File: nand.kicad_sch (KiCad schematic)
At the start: 5 parts, among them U6 IS21ES08GA-JQLI-TR

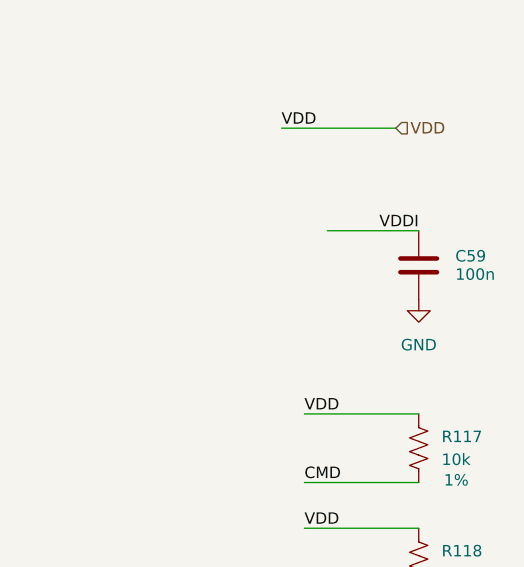
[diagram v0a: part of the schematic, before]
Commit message: Roughly placed all components
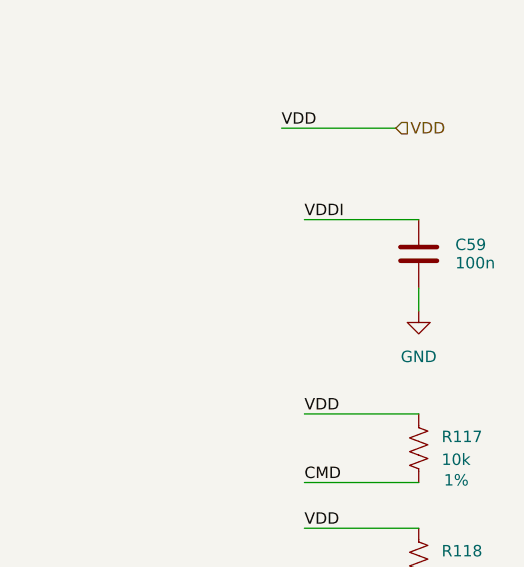
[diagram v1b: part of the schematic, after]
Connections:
- net GND: now also C59.2
- net VDDI: now also C59.1
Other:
- moved on the sheet: C59
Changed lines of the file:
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@@
 	(wire
 		(pts
-			(xy 246.3918 71.0847) (xy 256.5518 71.0847)
+			(xy 243.84 69.85) (xy 256.54 69.85)
 		)
 		(stroke
@@
 		(pts
 			(xy 168.91 101.6) (xy 168.91 104.14)
+		)
+		(stroke
+			(width 0)
+			(type default)
+		)
+	)
+	(wire
+		(pts
+			(xy 256.54 77.47) (xy 256.54 80.01)
 		)
 		(stroke
@@
 	)
 	(label "VDDI"
-		(at 256.5518 71.0847 180)
-		(fields_autoplaced yes)
-		(effects
-			(font
-				(size 1.27 1.27)
-			)
-			(justify right bottom)
+		(at 243.84 69.85 0)
+		(fields_autoplaced yes)
+		(effects
+			(font
+				(size 1.27 1.27)
+			)
+			(justify left bottom)
 		)
 	)
@@
 			)
 			(justify left)
+		)
+	)
+	(symbol
+		(lib_id "power:GND")
+		(at 256.54 80.01 0)
+		(unit 1)
+		(exclude_from_sim no)
+		(in_bom yes)
+		(on_board yes)
+		(dnp no)
+		(fields_autoplaced yes)
+		(property "Reference" "#PWR0218"
+			(at 256.54 86.36 0)
+			(effects
+				(font
+					(size 1.27 1.27)
+				)
+				(hide yes)
+			)
+		)
+		(property "Value" "GND"
+			(at 256.54 85.09 0)
+			(effects
+				(font
+					(size 1.27 1.27)
+				)
+			)
+		)
+		(property "Footprint" ""
+			(at 256.54 80.01 0)
+			(effects
+				(font
+					(size 1.27 1.27)
+				)
+				(hide yes)
+			)
+		)
+		(property "Datasheet" ""
+			(at 256.54 80.01 0)
+			(effects
+				(font
+					(size 1.27 1.27)
+				)
+				(hide yes)
+			)
+		)
+		(property "Description" "Power symbol creates a global label with name \"GND\" , ground"
+			(at 256.54 80.01 0)
+			(effects
+				(font
+					(size 1.27 1.27)
+				)
+				(hide yes)
+			)
+		)
+		(pin "1"
+		)
+		(instances
+			(project "SBC"
+				(path "/21bb932a-ec67-4661-9215-0551f718d1c0/dbc4538f-6782-4334-8773-c54462e4bd8b"
+					(reference "#PWR0218")
+					(unit 1)
+				)
+			)
 		)
 	)
@@
 	(symbol
 		(lib_id "SparkFun-Capacitor:C")
-		(at 256.54 74.93 0)
+		(at 256.54 73.66 0)
 		(unit 1)
 		(exclude_from_sim no)
@@
 		(dnp no)
 		(property "Reference" "C59"
-			(at 260.604 73.914 0)
+			(at 260.604 72.644 0)
 			(effects
 				(font
@@
 		)
 		(property "Value" "100n"
-			(at 260.604 75.946 0)
+			(at 260.604 74.676 0)
 			(effects
 				(font
@@
 		)
 		(property "Footprint" "Capacitor_SMD:C_0402_1005Metric"
-			(at 257.5052 86.36 0)
+			(at 257.5052 85.09 0)
 			(effects
 				(font
@@
 		)
 		(property "Datasheet" ""
-			(at 257.81 91.44 0)
+			(at 257.81 90.17 0)
 			(effects
 				(font
@@
 		)
 		(property "Description" "Unpolarized capacitor"
-			(at 256.54 93.98 0)
+			(at 256.54 92.71 0)
 			(effects
 				(font
@@
 		)
 		(property "PROD_ID" "CAP-00000"
-			(at 256.54 88.9 0)
+			(at 256.54 87.63 0)
 			(effects
 				(font
@@
 		)
 		(property "Voltage" ""
-			(at 260.35 76.1999 0)
+			(at 260.35 74.9299 0)
 			(effects
 				(font
@@
 					(unit 1)
 				)
-			)
-		)
-	)
-	(symbol
-		(lib_id "power:GND")
-		(at 256.5518 78.7047 0)
-		(unit 1)
-		(exclude_from_sim no)
-		(in_bom yes)
-		(on_board yes)
-		(dnp no)
-		(fields_autoplaced yes)
-		(property "Reference" "#PWR0218"
-			(at 256.5518 85.0547 0)
-			(effects
-				(font
-					(size 1.27 1.27)
-				)
-				(hide yes)
-			)
-		)
-		(property "Value" "GND"
-			(at 256.5518 83.7847 0)
-			(effects
-				(font
-					(size 1.27 1.27)
-				)
-			)
-		)
-		(property "Footprint" ""
-			(at 256.5518 78.7047 0)
-			(effects
-				(font
-					(size 1.27 1.27)
-				)
-				(hide yes)
-			)
-		)
-		(property "Datasheet" ""
-			(at 256.5518 78.7047 0)
-			(effects
-				(font
-					(size 1.27 1.27)
-				)
-				(hide yes)
-			)
-		)
-		(property "Description" "Power symbol creates a global label with name \"GND\" , ground"
-			(at 256.5518 78.7047 0)
-			(effects
-				(font
-					(size 1.27 1.27)
-				)
-				(hide yes)
-			)
-		)
-		(pin "1"
-		)
-		(instances
-			(project "SBC"
-				(path "/21bb932a-ec67-4661-9215-0551f718d1c0/dbc4538f-6782-4334-8773-c54462e4bd8b"
-					(reference "#PWR0218")
-					(unit 1)
-				)

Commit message: Routing routing routing
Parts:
- removed C59: 100n, Capacitor_SMD:C_0402_1005Metric, symbol SparkFun-Capacitor:C
- added C89, C90: 4.7u, Capacitor_SMD:C_0603_1608Metric, symbol SparkFun-Capacitor:C
- added C91: 1uF, Capacitor_SMD:C_0402_1005Metric, symbol SparkFun-Capacitor:C
- added R145: 10k, Capacitor_SMD:C_0402_1005Metric, symbol SparkFun-Resistor:R
- R117, R118, R119: Precision 1% -> 5%
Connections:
- net GND: now also C89.2, C90.2, C91.2, R145.2
- net VDD: now also C89.1, C90.1; no longer U6.E4 (VDDI)
- net VDDI: now also U6.E4 (VDDI), C91.1
- net DS: now reaches U6.K5 (DS)
- net DS: now also R145.1
- no-connect marks 1 -> 0

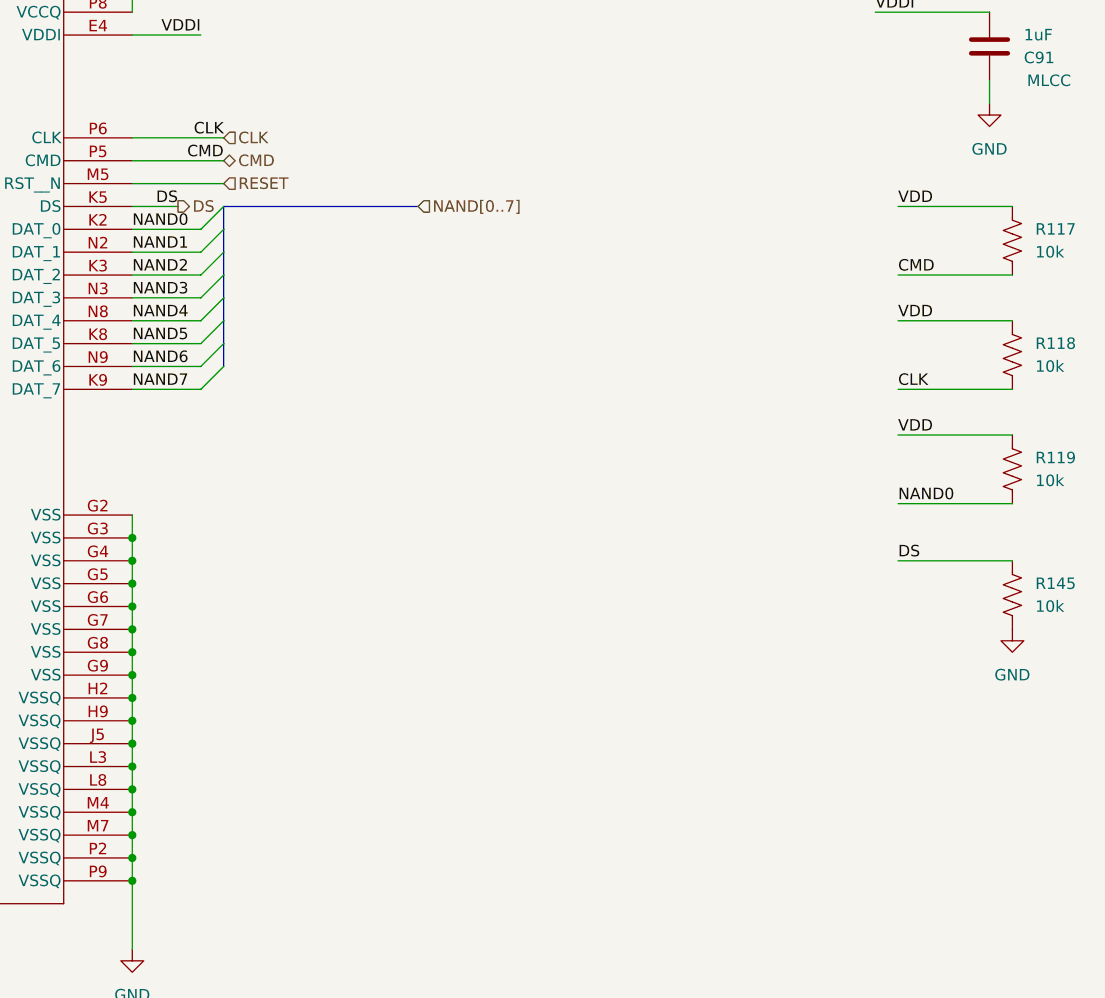
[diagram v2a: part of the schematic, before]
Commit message: eMMC routing done
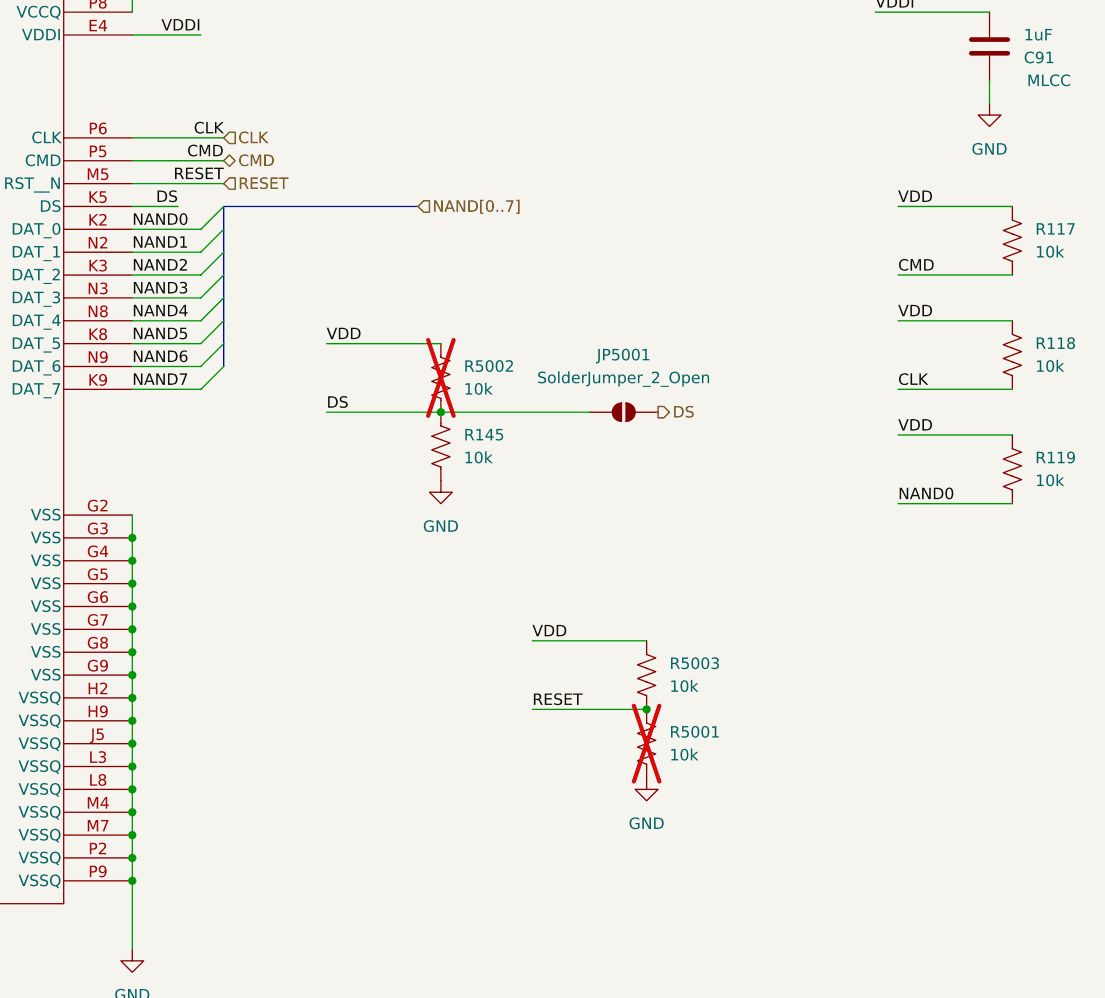
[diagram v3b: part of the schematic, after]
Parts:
- added JP5001: SolderJumper_2_Open, SparkFun-Jumper:Jumper_2_NO, symbol Jumper:SolderJumper_2_Open
- added R5001, R5002, R5003: 10k, Capacitor_SMD:C_0402_1005Metric, symbol SparkFun-Resistor:R
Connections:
- net DS: now also JP5001.1 (A), JP5001.2 (B), R5002.2
- net GND: now also R5001.2
- net RESET: now also R5001.1, R5003.2
- net VDD: now also R5002.1, R5003.1
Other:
- moved on the sheet: R145

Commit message: Ethernet routing
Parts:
- R117, R118, R119, R145, R5001, R5002, R5003: footprint Capacitor_SMD:C_0402_1005Metric -> Resistor_SMD:R_0402_1005Metric
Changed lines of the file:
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@@
 			)
 		)
-		(property "Footprint" "Capacitor_SMD:C_0402_1005Metric"
+		(property "Footprint" "Resistor_SMD:R_0402_1005Metric"
 			(at 261.112 107.95 0)
 			(effects
@@
 			)
 		)
-		(property "Footprint" "Capacitor_SMD:C_0402_1005Metric"
+		(property "Footprint" "Resistor_SMD:R_0402_1005Metric"
 			(at 220.472 143.51 0)
 			(effects
@@
 			)
 		)
-		(property "Footprint" "Capacitor_SMD:C_0402_1005Metric"
+		(property "Footprint" "Resistor_SMD:R_0402_1005Metric"
 			(at 261.112 120.65 0)
 			(effects
@@
 			)
 		)
-		(property "Footprint" "Capacitor_SMD:C_0402_1005Metric"
+		(property "Footprint" "Resistor_SMD:R_0402_1005Metric"
 			(at 197.612 110.49 0)
 			(effects
@@
 			)
 		)
-		(property "Footprint" "Capacitor_SMD:C_0402_1005Metric"
+		(property "Footprint" "Resistor_SMD:R_0402_1005Metric"
 			(at 261.112 95.25 0)
 			(effects
@@
 			)
 		)
-		(property "Footprint" "Capacitor_SMD:C_0402_1005Metric"
+		(property "Footprint" "Resistor_SMD:R_0402_1005Metric"
 			(at 197.612 118.11 0)
 			(effects
@@
 			)
 		)
-		(property "Footprint" "Capacitor_SMD:C_0402_1005Metric"
+		(property "Footprint" "Resistor_SMD:R_0402_1005Metric"
 			(at 220.472 151.13 0)
 			(effects

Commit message: Initial routing complete
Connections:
- net DS: no longer JP5001.1 (A), R145.1, R5002.2, U6.K5 (DS)
- new net DS_NAND: JP5001.1 (A), R145.1, R5002.2, U6.K5 (DS)
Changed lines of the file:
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@@
 	(wire
 		(pts
-			(xy 158.75 91.44) (xy 163.83 91.44)
+			(xy 158.75 91.44) (xy 167.64 91.44)
 		)
 		(stroke
@@
 		)
 	)
-	(label "DS"
+	(label "DS_NAND"
 		(at 180.34 114.3 0)
 		(fields_autoplaced yes)
@@
 		)
 	)
-	(label "DS"
-		(at 163.83 91.44 180)
-		(fields_autoplaced yes)
-		(effects
+	(label "DS_NAND"
+		(at 167.64 91.44 180)
+		(fields_autoplaced yes)
+		(effects

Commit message: Started an entire reroute
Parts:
- removed JP5001: SolderJumper_2_Open, SparkFun-Jumper:Jumper_2_NO, symbol Jumper:SolderJumper_2_Open
- added JP4: SolderJumper_2_Open, Jumper:SolderJumper-2_P1.3mm_Open_Pad1.0x1.5mm, symbol Jumper:SolderJumper_2_Open
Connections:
- net DS: now also JP4.2 (B)
- net DS_NAND: now also JP4.1 (A)
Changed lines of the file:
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@@
 (kicad_sch
-	(version 20231120)
+	(version 20250114)
 	(generator "eeschema")
-	(generator_version "8.0")
+	(generator_version "9.0")
 	(paper "A4")
 	(junction
@@
 	(label "VDD"
 		(at 168.91 25.4 180)
-		(fields_autoplaced yes)
 		(effects
 			(font
@@
 	(label "CMD"
 		(at 243.84 99.06 0)
-		(fields_autoplaced yes)
 		(effects
 			(font
@@
 	(label "CLK"
 		(at 168.91 83.82 180)
-		(fields_autoplaced yes)
 		(effects
 			(font
@@
 	(label "NAND0"
 		(at 243.84 124.46 0)
-		(fields_autoplaced yes)
 		(effects
 			(font
@@
 	(label "VDD"
 		(at 241.3 59.69 0)
-		(fields_autoplaced yes)
 		(effects
 			(font
@@
 	(label "VDDI"
 		(at 166.37 72.39 180)
-		(fields_autoplaced yes)
 		(effects
 			(font
@@
 	(label "DS_NAND"
 		(at 180.34 114.3 0)
-		(fields_autoplaced yes)
 		(effects
 			(font
@@
 	(label "RESET"
 		(at 168.91 88.9 180)
-		(fields_autoplaced yes)
 		(effects
 			(font
@@
 	(label "DS_NAND"
 		(at 167.64 91.44 180)
-		(fields_autoplaced yes)
 		(effects
 			(font
@@
 	(label "RESET"
 		(at 203.2 147.32 0)
-		(fields_autoplaced yes)
 		(effects
 			(font
@@
 	(label "VDD"
 		(at 243.84 116.84 0)
-		(fields_autoplaced yes)
 		(effects
 			(font
@@
 	(label "VDD"
 		(at 180.34 106.68 0)
-		(fields_autoplaced yes)
 		(effects
 			(font
@@
 	(label "NAND2"
 		(at 158.75 99.06 0)
-		(fields_autoplaced yes)
 		(effects
 			(font
@@
 	(label "VDD"
 		(at 243.84 104.14 0)
-		(fields_autoplaced yes)
 		(effects
 			(font
@@
 	(label "CMD"
 		(at 168.91 86.36 180)
-		(fields_autoplaced yes)
 		(effects
 			(font
@@
 	(label "NAND7"
 		(at 158.75 111.76 0)
-		(fields_autoplaced yes)
 		(effects
 			(font
@@
 	(label "VDD"
 		(at 203.2 139.7 0)
-		(fields_autoplaced yes)
 		(effects
 			(font
@@
 	(label "VDDI"
 		(at 241.3 69.85 0)
-		(fields_autoplaced yes)
 		(effects
 			(font
@@
 	(label "CLK"
 		(at 243.84 111.76 0)
-		(fields_autoplaced yes)
 		(effects
 			(font
@@
 	(label "VDD"
 		(at 243.84 91.44 0)
-		(fields_autoplaced yes)
 		(effects
 			(font
@@
 	(label "NAND3"
 		(at 158.75 101.6 0)
-		(fields_autoplaced yes)
 		(effects
 			(font
@@
 	(label "NAND4"
 		(at 158.75 104.14 0)
-		(fields_autoplaced yes)
 		(effects
 			(font
@@
 	(label "NAND1"
 		(at 158.75 96.52 0)
-		(fields_autoplaced yes)
 		(effects
 			(font
@@
 	(label "NAND6"
 		(at 158.75 109.22 0)
-		(fields_autoplaced yes)
 		(effects
 			(font
@@
 	(label "NAND0"
 		(at 158.75 93.98 0)
-		(fields_autoplaced yes)
 		(effects
 			(font
@@
 	(label "NAND5"
 		(at 158.75 106.68 0)
-		(fields_autoplaced yes)
 		(effects
 			(font
@@
 		(shape output)
 		(at 217.17 114.3 0)
-		(fields_autoplaced yes)
 		(effects
 			(font
@@
 		(shape input)
 		(at 254 59.69 0)
-		(fields_autoplaced yes)
 		(effects
 			(font
@@
 		(shape bidirectional)
 		(at 168.91 86.36 0)
-		(fields_autoplaced yes)
 		(effects
 			(font
@@
 		(shape input)
 		(at 168.91 83.82 0)
-		(fields_autoplaced yes)
 		(effects
 			(font
@@
 		(shape input)
 		(at 168.91 88.9 0)
-		(fields_autoplaced yes)
 		(effects
 			(font
@@
 		(shape input)
 		(at 190.5 91.44 0)
-		(fields_autoplaced yes)
 		(effects
 			(font
@@
 	)
 	(symbol
-		(lib_id "Jumper:SolderJumper_2_Open")
-		(at 213.36 114.3 0)
-		(unit 1)
-		(exclude_from_sim yes)
-		(in_bom no)
-		(on_board yes)
-		(dnp no)
-		(fields_autoplaced yes)
-		(property "Reference" "JP5001"
-			(at 213.36 107.95 0)
-			(effects
-				(font
-					(size 1.27 1.27)
-				)
-			)
-		)
-		(property "Value" "SolderJumper_2_Open"
-			(at 213.36 110.49 0)
-			(effects
-				(font
-					(size 1.27 1.27)
-				)
-			)
-		)
-		(property "Footprint" "SparkFun-Jumper:Jumper_2_NO"
-			(at 213.36 114.3 0)
-			(effects
-				(font
-					(size 1.27 1.27)
-				)
-				(hide yes)
-			)
-		)
-		(property "Datasheet" "~"
-			(at 213.36 114.3 0)
-			(effects
-				(font
-					(size 1.27 1.27)
-				)
-				(hide yes)
-			)
-		)
-		(property "Description" "Solder Jumper, 2-pole, open"
-			(at 213.36 114.3 0)
-			(effects
-				(font
-					(size 1.27 1.27)
-				)
-				(hide yes)
-			)
-		)
-		(pin "1"
-		)
-		(pin "2"
-		)
-		(instances
-			(project "SBC"
-				(path "/21bb932a-ec67-4661-9215-0551f718d1c0/dbc4538f-6782-4334-8773-c54462e4bd8b"
-					(reference "JP5001")
-					(unit 1)
-				)
-			)
-		)
-	)
-	(symbol
 		(lib_id "SparkFun-Resistor:R")
 		(at 256.54 95.25 90)
@@
 					(unit 1)
 				)
+			)
+		)
+	)
+	(symbol
+		(lib_name "SolderJumper_2_Open_1")
+		(lib_id "Jumper:SolderJumper_2_Open")
+		(at 213.36 114.3 0)
+		(unit 1)
+		(exclude_from_sim no)
+		(in_bom no)
+		(on_board yes)
+		(dnp no)
+		(fields_autoplaced yes)
+		(property "Reference" "JP4"
+			(at 213.36 107.95 0)
+			(effects
+				(font
+					(size 1.27 1.27)
+				)
+			)
+		)
+		(property "Value" "SolderJumper_2_Open"
+			(at 213.36 110.49 0)
+			(effects
+				(font
+					(size 1.27 1.27)
+				)
+			)
+		)
+		(property "Footprint" "Jumper:SolderJumper-2_P1.3mm_Open_Pad1.0x1.5mm"
+			(at 213.36 114.3 0)
+			(effects
+				(font
+					(size 1.27 1.27)
+				)
+				(hide yes)
+			)
+		)
+		(property "Datasheet" "~"
+			(at 213.36 114.3 0)
+			(effects
+				(font
+					(size 1.27 1.27)
+				)
+				(hide yes)
+			)
+		)
+		(property "Description" "Solder Jumper, 2-pole, open"
+			(at 213.36 114.3 0)
+			(effects
+				(font
+					(size 1.27 1.27)
+				)
+				(hide yes)
+			)
+		)
+		(pin "2"
+		)
+		(pin "1"
+		)
+		(instances
+			(project ""
+				(path "/21bb932a-ec67-4661-9215-0551f718d1c0/dbc4538f-6782-4334-8773-c54462e4bd8b"
+					(reference "JP4")
+					(unit 1)
+				)
